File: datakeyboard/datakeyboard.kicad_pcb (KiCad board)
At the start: 2 copper layers, 58 x 41 mm, 42 parts, among them Q1 BSS83P, Q2 BSS83P, Q3 BSS83P, SW1 SW_Push, SW2 SW_Push, SW3 SW_Push, SW4 SW_Push, SW5 SW_Push, SW6 SW_Push, U1 PIC24FJ128GB204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

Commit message: Start board layout
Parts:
- JBAT1, JCASE1: footprint Connector_PinHeader_2.54mm:PinHeader_1x02_P2.54mm_Vertical -> Resistor_SMD:R_1206_3216Metric_Pad1.30x1.75mm_HandSolder
- JCARD1: footprint Connector_Card:microSD_HC_Hirose_DM3AT-SF-PEJM5 -> Library:microSD_Unknown
- JUSB1: footprint Connector_USB:USB_Micro-B_Molex-105017-0001 -> Library:USB_Micro-B_Unknown
- moved C4 39.2 mm to (143.7, 122.6)
- moved C5 31.5 mm to (106.6, 112.9), turned to 90 degrees
- moved C10 11.6 mm to (123.0, 117.6)
- moved C11 9.52 mm to (126.2, 107.9)
- moved R10 3.50 mm to (123.5, 131.0)
- moved R11 3.50 mm to (123.5, 126.5)
- moved Q1 2.55 mm to (120.5, 130.9)
- moved Q2 2.55 mm to (120.5, 126.5)
- moved JCARD1 2.47 mm to (107.0, 137.0)
- moved JBAT1 2.21 mm to (135.4, 132.5), turned to 180 degrees
- moved R7 1.50 mm to (128.5, 108.0), turned to 90 degrees
- moved C3 1.21 mm to (106.7, 117.2)
- moved JCASE1 1.12 mm to (106.5, 125.0), turned to 180 degrees
- moved Q3 1.00 mm to (136.0, 108.0)
- moved JUSB1 0.75 mm to (154.2, 138.5)
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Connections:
- JCARD1 pad 10: /SDCard_CD -> unconnected-(JCARD1-Pad10)
- JCARD1 pad 9: unconnected-(JCARD1-Pad9) -> /SDCard_CD
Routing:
- net +3V0: track 0.00 -> 82.0 mm
- net /VUSB: track 0.00 -> 55.6 mm, vias 0 -> 1
- net /VBAT: track 0.00 -> 45.7 mm
- net GND: track 0.00 -> 26.3 mm, vias 0 -> 11
- net /LEDA: track 0.00 -> 19.1 mm
- net /RESET: track 0.00 -> 10.6 mm
- net Net-(Q3-Pad3): track 0.00 -> 9.41 mm
- net /VPER: track 0.00 -> 9.24 mm
- net Net-(C11-Pad1): track 0.00 -> 5.33 mm
- net /VOLT_PWR: track 0.00 -> 4.53 mm
- net Net-(R9-Pad2): track 0.00 -> 3.76 mm
- net /VOLT_READ: track 0.00 -> 3.00 mm
- net Net-(C3-Pad2): track 0.00 -> 2.60 mm
- added copper zone on F.Cu, net GND

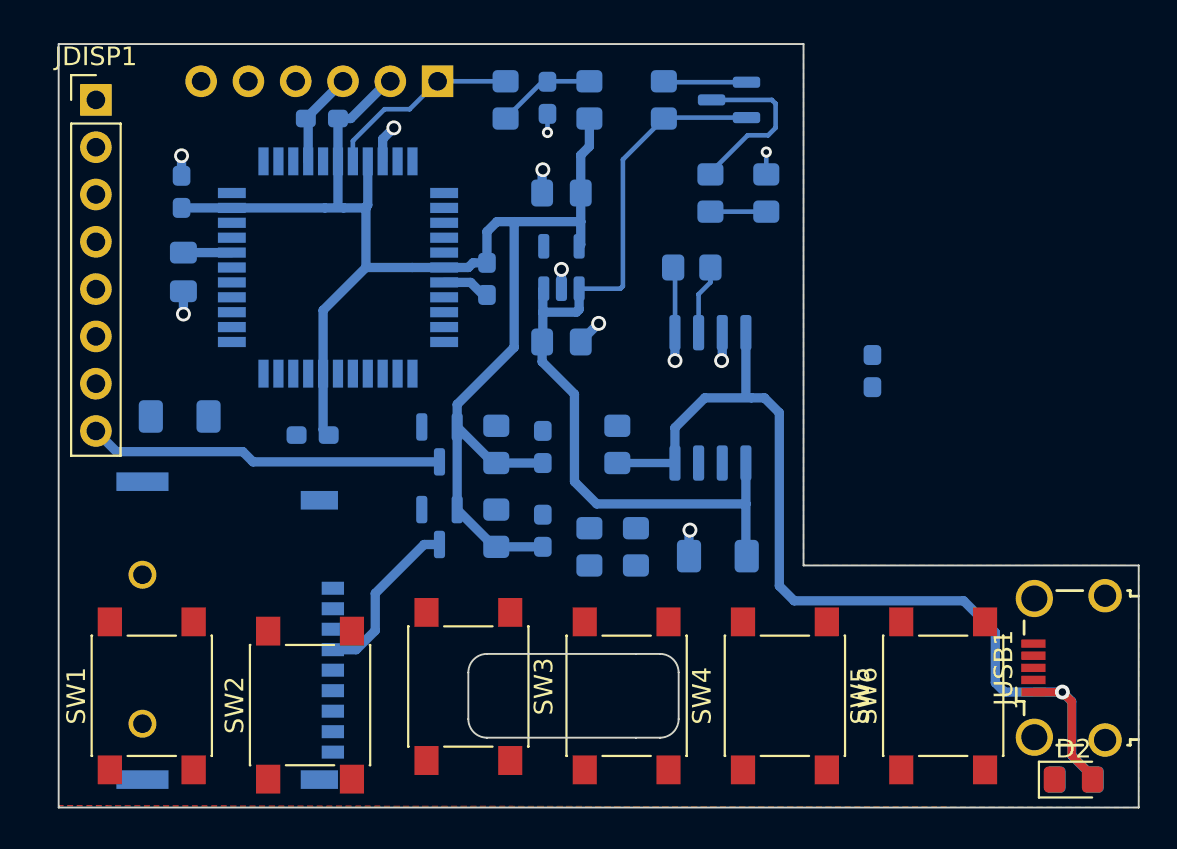
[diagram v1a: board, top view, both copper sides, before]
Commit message: Finish PCB layout
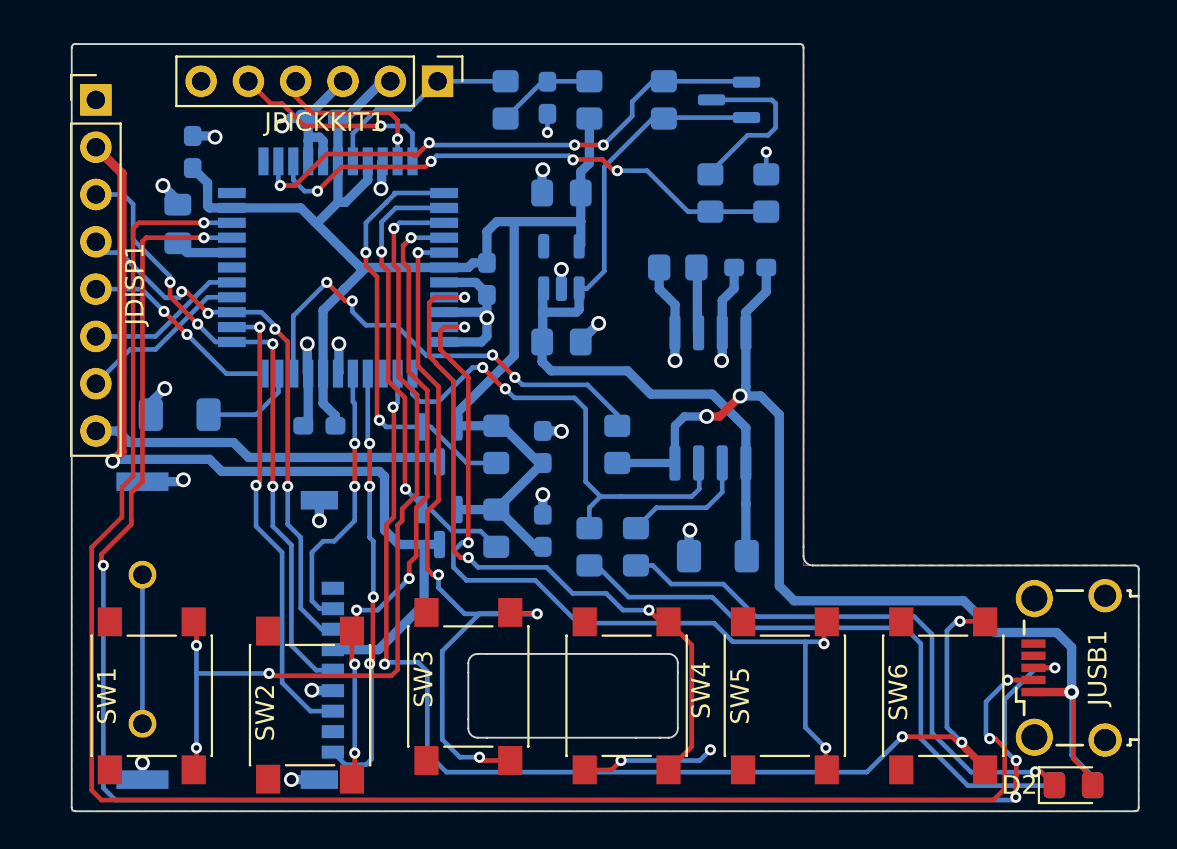
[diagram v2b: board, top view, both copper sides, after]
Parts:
- JPICKKIT1: moved to F.Cu
- moved C4 8.60 mm to (137.1, 117.0), turned to 0 degrees
- moved C3 2.59 mm to (106.4, 114.7), turned to -90 degrees
- moved C5 2.22 mm to (107.2, 110.8)
- moved R9 0.75 mm to (133.2, 117.0)
- moved C8 0.62 mm to (114.0, 125.5)
- moved D1 0.30 mm to (154.5, 144.8)
- moved D2 0.30 mm to (154.5, 144.8)
- moved JCASE1 0.10 mm to (106.5, 124.9)
- turned JPICKKIT1 to -90 degrees
- turned R10 to 90 degrees
- turned R11 to -90 degrees
- turned SW3 to 90 degrees
- turned SW4 to 90 degrees
- turned SW5 to 90 degrees
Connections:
- R2 pad 2: Net-(R2-Pad2) -> /CHRG
- SW4 pad 2: /BNT4 -> /BTN4
- U1 pad 34: GND -> /CHRG
- U2 pad 7: Net-(R2-Pad2) -> /CHRG
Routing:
- net Net-(JUSB1-Pad3): track 0.00 -> 94.6 mm, vias 0 -> 5
- net Net-(JUSB1-Pad2): track 0.00 -> 94.3 mm, vias 0 -> 3
- net /BTN6: track 0.00 -> 65.3 mm, vias 0 -> 5
- net /BTN1: track 0.00 -> 46.5 mm, vias 0 -> 4
- net /BTN5: track 0.00 -> 46.5 mm, vias 0 -> 4
- net /BTN3: track 0.00 -> 42.7 mm, vias 0 -> 4
- net /BTN4: track 0.00 -> 39.1 mm, vias 0 -> 3
- net /VPER: track 9.24 -> 47.9 mm, vias 0 -> 1
- net GND: track 26.3 -> 65.0 mm, vias 11 -> 25
- net /BTN2: track 0.00 -> 34.0 mm, vias 0 -> 5
- net /SCLK: track 0.00 -> 34.0 mm, vias 0 -> 4
- net Net-(D1-Pad1): track 0.00 -> 33.3 mm
- net Net-(D2-Pad1): track 0.00 -> 30.5 mm, vias 0 -> 1
- net /MOSI: track 0.00 -> 29.9 mm, vias 0 -> 4
- net /CHRG: track 0.00 -> 26.1 mm, vias 0 -> 2
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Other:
- board size 58 x 41 mm -> 57.3 x 41.2 mm
- board text added: "CASE"
- board text added: "GND"
- board text added: "VBAT"
